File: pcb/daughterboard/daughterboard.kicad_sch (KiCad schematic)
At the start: 0 parts

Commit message: initial daughterboard design
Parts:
- added J1: Conn_02x20_Counter_Clockwise, symbol Connector_Generic:Conn_02x20_Counter_Clockwise
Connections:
- new net +3.3V: J1.39 (Pin_39)
- new net +9V: J1.40 (Pin_40)
- new net GND: J1.38 (Pin_38)
- new net drivers1/SPI_CS: J1.3 (Pin_3)
- new net drivers1/SPI_MOSI: J1.1 (Pin_1)
- new net drivers1/SPI_SCLK: J1.2 (Pin_2)
- new net drivers2/SPI_MISO: J1.4 (Pin_4)
- no-connect marks 0 -> 33
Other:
- added sheet drivers1 (drivers1.kicad_sch)
- added sheet drivers2 (drivers2.kicad_sch)
- added sheet motors (motors.kicad_sch)

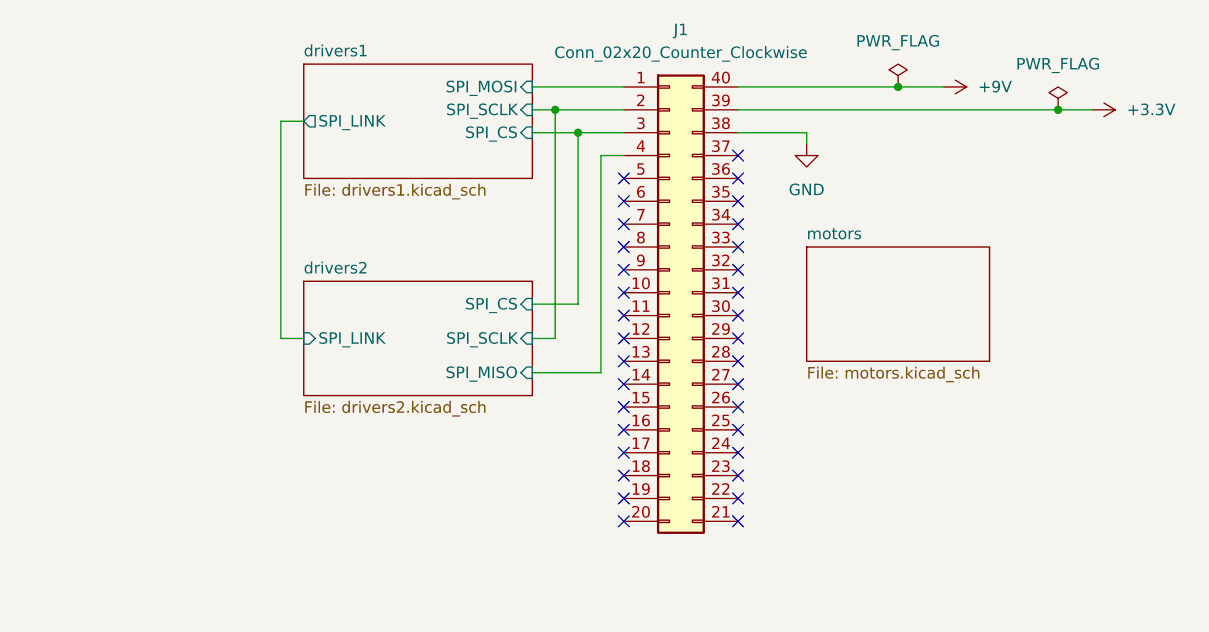
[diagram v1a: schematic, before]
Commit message: added footprints
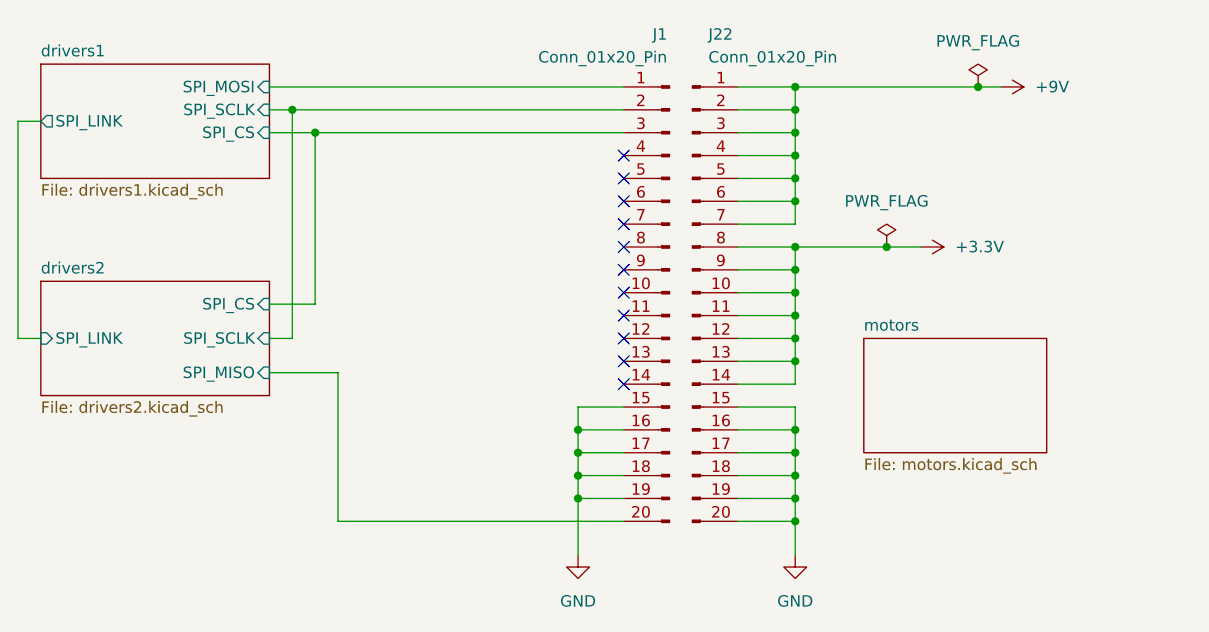
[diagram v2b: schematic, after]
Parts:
- removed J1: Conn_02x20_Counter_Clockwise, symbol Connector_Generic:Conn_02x20_Counter_Clockwise
- added J1, J22: Conn_01x20_Pin, Connector_PinHeader_2.54mm:PinHeader_1x20_P2.54mm_Horizontal, symbol Connector:Conn_01x20_Pin
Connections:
- net +3.3V: now also J22.10 (Pin_10), J22.11 (Pin_11), J22.12 (Pin_12), J22.13 (Pin_13), J22.14 (Pin_14), J22.8 (Pin_8), J22.9 (Pin_9)
- net +9V: now also J22.1 (Pin_1), J22.2 (Pin_2), J22.3 (Pin_3), J22.4 (Pin_4), J22.5 (Pin_5), J22.6 (Pin_6), J22.7 (Pin_7)
- net GND: now also J1.15 (Pin_15), J1.16 (Pin_16), J1.17 (Pin_17), J1.18 (Pin_18), J1.19 (Pin_19), J22.15 (Pin_15), J22.16 (Pin_16), J22.17 (Pin_17), J22.18 (Pin_18), J22.19 (Pin_19), J22.20 (Pin_20)
- net drivers1/SPI_CS: now also J1.3 (Pin_3)
- net drivers1/SPI_MOSI: now also J1.1 (Pin_1)
- net drivers1/SPI_SCLK: now also J1.2 (Pin_2)
- net drivers2/SPI_MISO: now also J1.20 (Pin_20)
- no-connect marks 33 -> 11
